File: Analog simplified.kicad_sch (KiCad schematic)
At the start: 20 parts, among them U3 74HC4051, U4 74HC4051, U5 OPA350

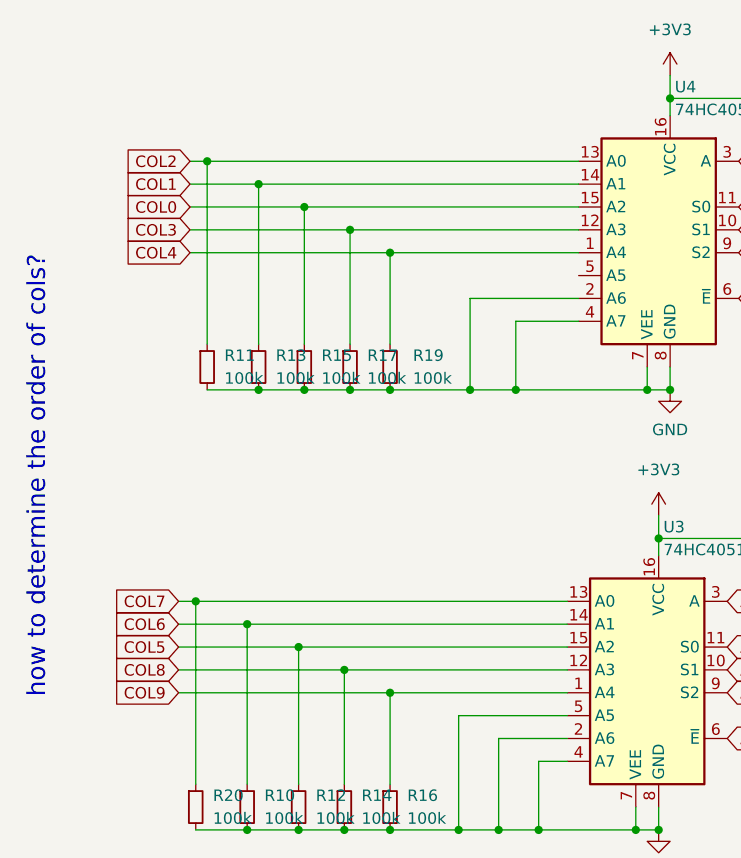
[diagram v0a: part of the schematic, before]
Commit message: created more plates
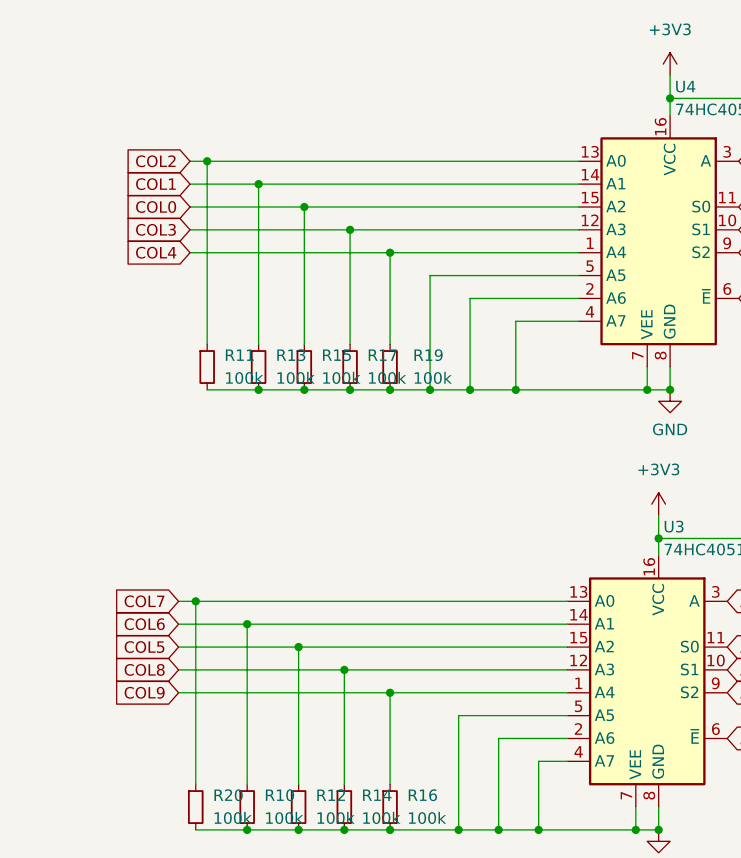
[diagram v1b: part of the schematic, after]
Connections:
- net GND: now also U4.5 (A5)
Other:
- note removed: "how to determine the order of cols?"
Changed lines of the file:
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@@
   (junction (at 69.85 42.545) (diameter 0) (color 0 0 0 0)
   )
+  (junction (at 94.615 67.945) (diameter 0) (color 0 0 0 0)
+  )
   (junction (at 80.01 96.52) (diameter 0) (color 0 0 0 0)
   )
@@
     (stroke (width 0) (type default))
   )
-  (wire (pts (xy 90.17 67.945) (xy 99.06 67.945))
+  (wire (pts (xy 94.615 55.245) (xy 94.615 67.945))
+    (stroke (width 0) (type default))
+  )
+  (wire (pts (xy 90.17 67.945) (xy 94.615 67.945))
     (stroke (width 0) (type default))
   )
@@
     (stroke (width 0) (type default))
   )
+  (wire (pts (xy 94.615 67.945) (xy 99.06 67.945))
+    (stroke (width 0) (type default))
+  )
   (wire (pts (xy 249.555 46.99) (xy 254 46.99))
     (stroke (width 0) (type default))
@@
     (stroke (width 0) (type default))
   )
+  (wire (pts (xy 111.125 55.245) (xy 94.615 55.245))
+    (stroke (width 0) (type default))
+  )
   (wire (pts (xy 134.62 86.36) (xy 134.62 84.455))
     (stroke (width 0) (type default))
@@
     (stroke (width 0) (type default))
   )
-  (text "how to determine the order of cols?" (at 52.07 102.235 90)
-    (effects (font (size 2 2)) (justify left bottom))
-  )
   (global_label "APLEX_EN_PIN_1" (shape input) (at 127.635 106.68 0) (fields_autoplaced)
